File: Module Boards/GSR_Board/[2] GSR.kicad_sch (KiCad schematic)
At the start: 27 parts, among them U1 AD8236ARMZ-R7, U2 LTC2064IDD#PBF, U3 MAX5419LETA+T, U4 MAX5419LETA+T

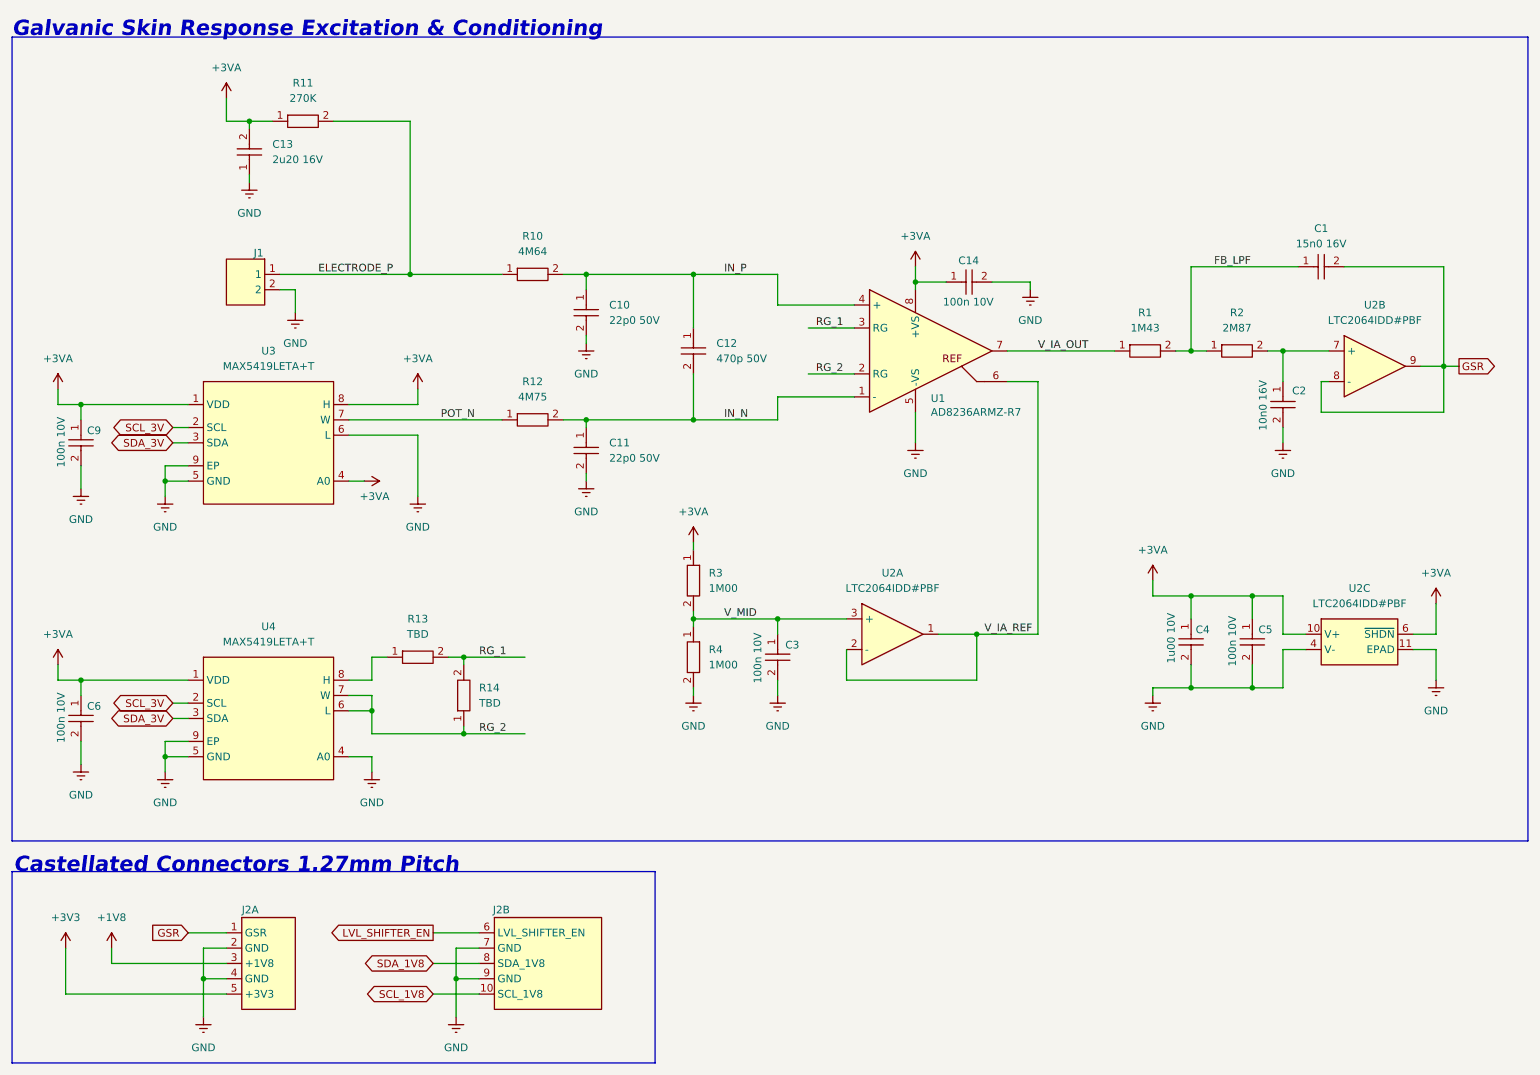
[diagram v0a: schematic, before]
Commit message: Added ADC to board and partially placed/routed the updated board
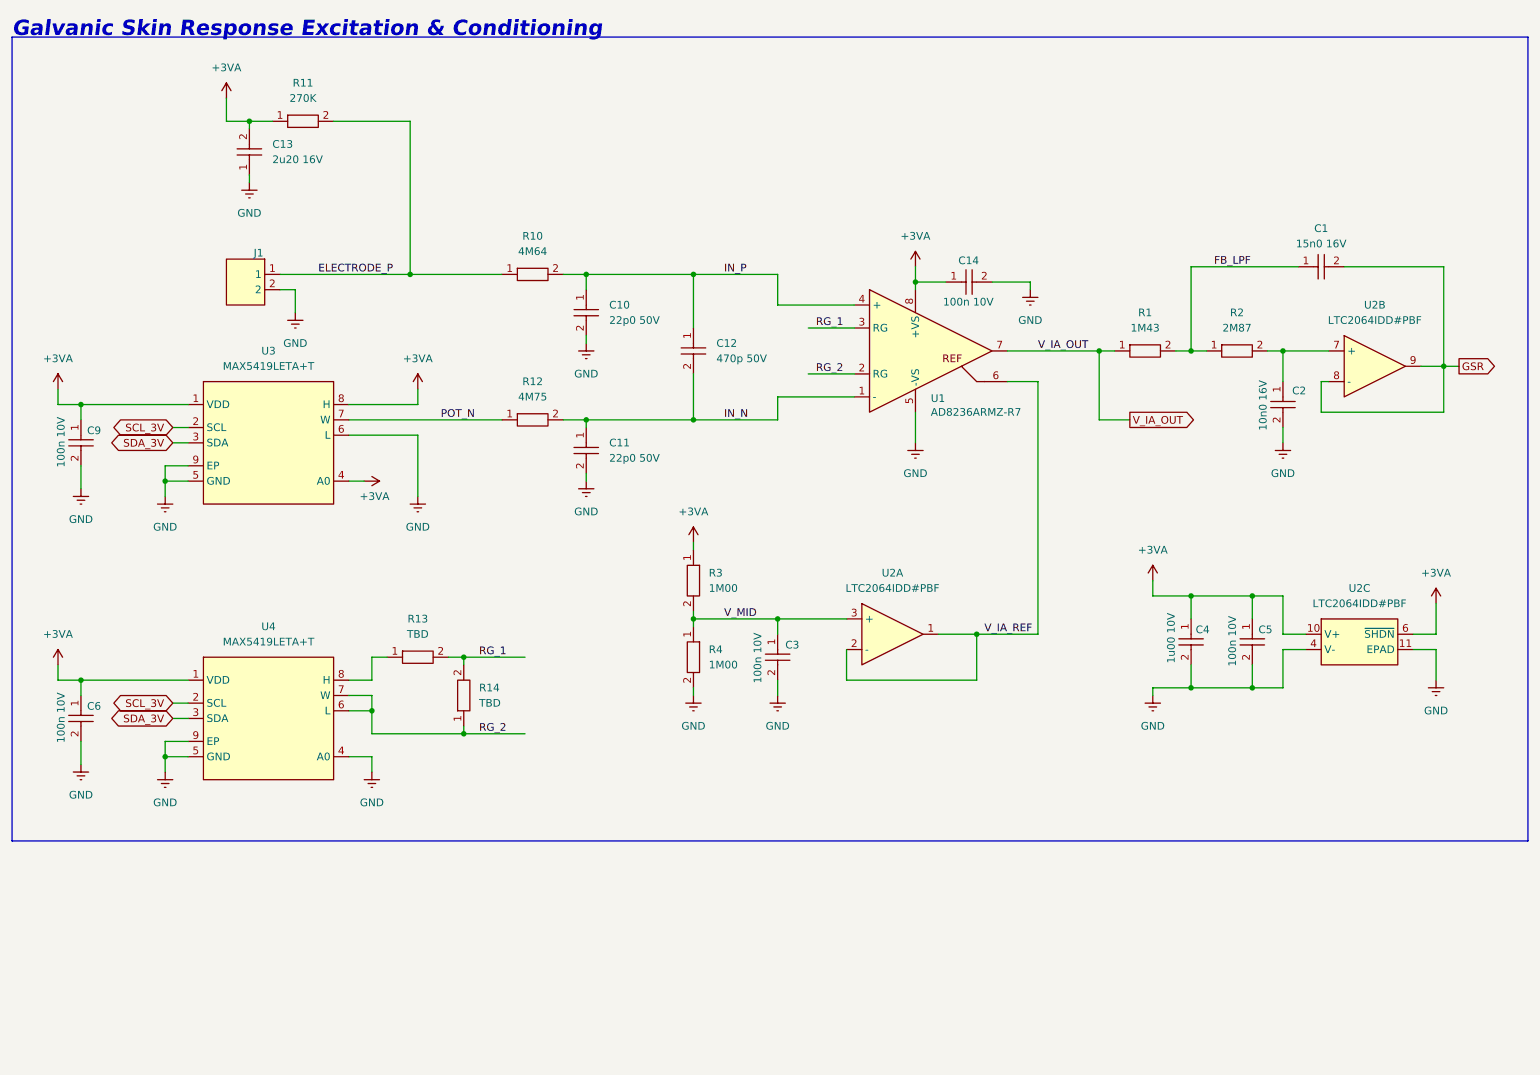
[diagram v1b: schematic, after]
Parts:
- removed J2: ~, X-MODs_PcbLib:GSR_Board_Castellated_Conn_1.27mm, symbol X-MODs_SchLib:GSR_Board_Castellated_Conn_1.27mm
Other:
- note removed: "Castellated Connectors 1.27mm Pitch"

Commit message: Finished Routing of GSR Board
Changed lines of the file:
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@@
 	(text "Galvanic Skin Response Excitation & Conditioning"
 		(exclude_from_sim no)
-		(at 22.86 21.59 0)
+		(at 23.368 21.59 0)
 		(effects
 			(font
